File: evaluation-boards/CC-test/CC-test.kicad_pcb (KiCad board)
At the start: 2 copper layers, 30 x 26.3 mm, 27 parts, among them J1 Conn_02x06_Top_Bottom, J2 Conn_01x02, J3 Conn_01x02, J4 Conn_01x02, J5 Conn_01x02, J6 USB_C_Receptacle_USB2.0, J7 Conn_01x02, J8 Conn_01x02, U1 MIC5504-1.8YM5, U2 74AUP2G126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

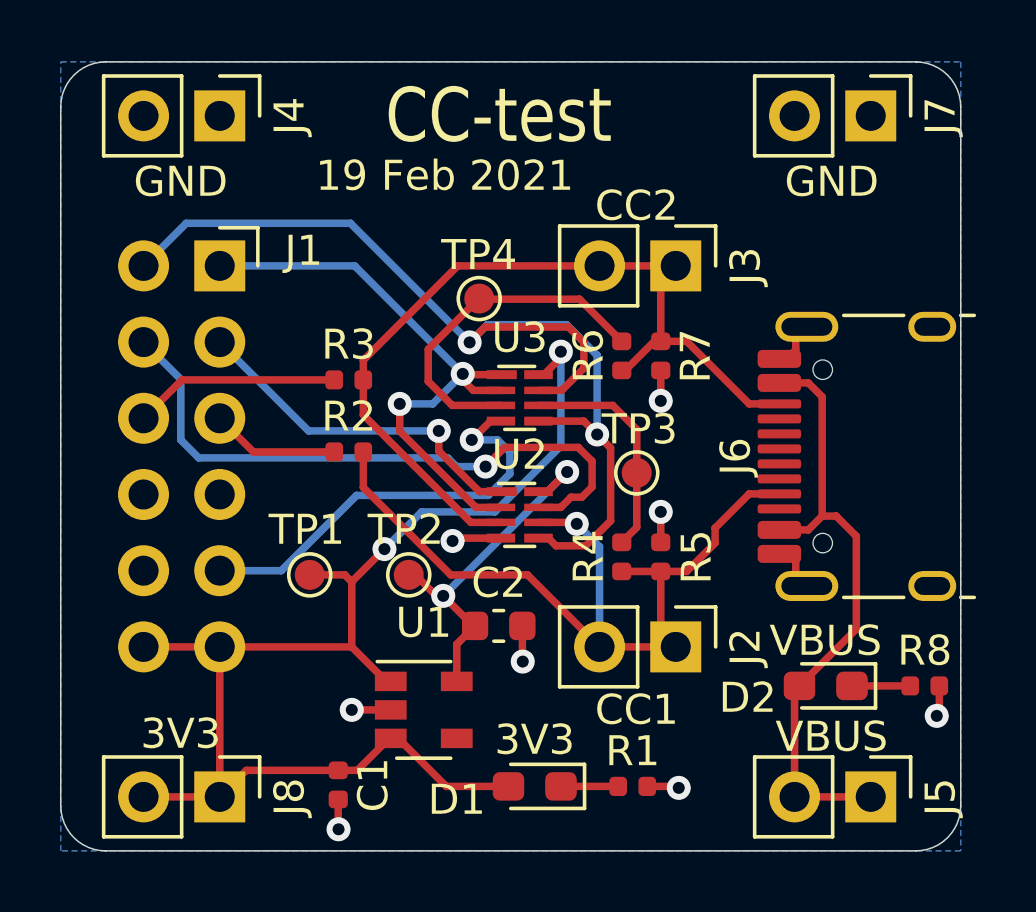
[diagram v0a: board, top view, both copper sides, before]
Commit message: CC-test: change U2 and U3 to 74AUP2G126RA3-7
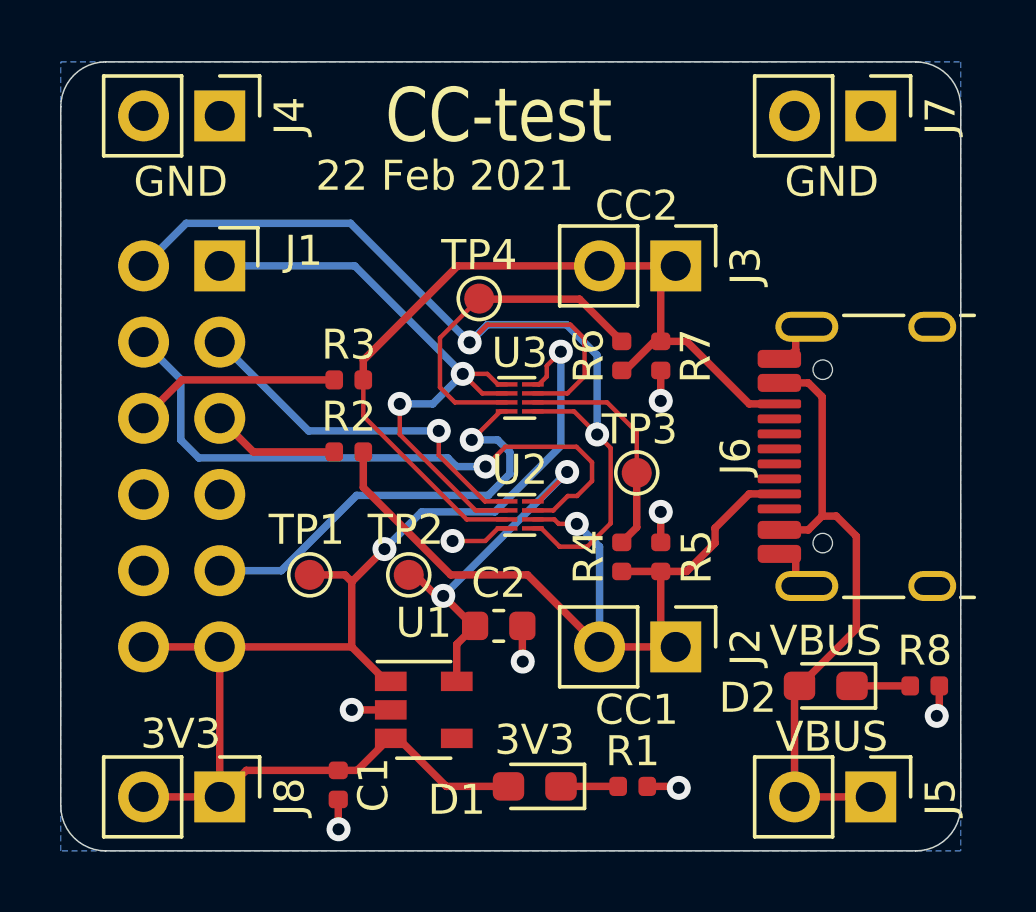
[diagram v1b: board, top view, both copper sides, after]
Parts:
- U2, U3: footprint CC-test:XSON-8_1.95x1mm_P0.5mm -> CC-test:X2-DFN1210-8_1.2x1mm_P0.3mm
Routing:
- net /CC2_OUTPUT: track 35.6 -> 36.9 mm
- net /CC1_OUTPUT: track 20.4 -> 21.3 mm
- net GND: track 26.9 -> 27.6 mm
- net +3V3: track 44.2 -> 44.8 mm
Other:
- net class Default: clearance 0.2 -> 0.15; trace_width 0.25 -> 0.15
- rule trace_clearance: 0.2 -> 0.15
- rule trace_min: 0.2 -> 0.15
- rule via_min_drill: 0.3 -> 0.254
- rule via_min_size: 0.4 -> 0.508
- board text added: "22 Feb 2021"
- board text removed: "19 Feb 2021"
